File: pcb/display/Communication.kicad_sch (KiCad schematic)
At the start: 12 parts, among them U5 SP3485EN, U7 Ai-Thinker-Ra-02, U8 E220-400M22S

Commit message: Final Version of Prototype Rev. 00
Switched back to PCA9685 for PWM, removed high side switch
Updated some component values
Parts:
- R11, U7: now not fitted
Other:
- note removed: "OK!"
- title: (none) -> Communication
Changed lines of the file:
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@@
 	(paper "A4")
 	(title_block
-		(date "2024-11-11")
+		(title "Communication")
+		(date "2024-11-17")
 		(rev "00")
 		(company "Ravenspark")
@@
 			(width 0)
 			(type default)
-		)
-	)
-	(text "OK!"
-		(exclude_from_sim no)
-		(at 146.05 41.91 0)
-		(effects
-			(font
-				(size 2.54 2.54)
-				(thickness 0.254)
-				(bold yes)
-				(color 255 176 0 1)
-			)
 		)
 	)
@@
 		(in_bom yes)
 		(on_board yes)
-		(dnp no)
+		(dnp yes)
 		(fields_autoplaced yes)
 		(property "Reference" "U7"
@@
 		(in_bom yes)
 		(on_board yes)
-		(dnp no)
+		(dnp yes)
 		(property "Reference" "R11"
 			(at 95.25 146.05 90)

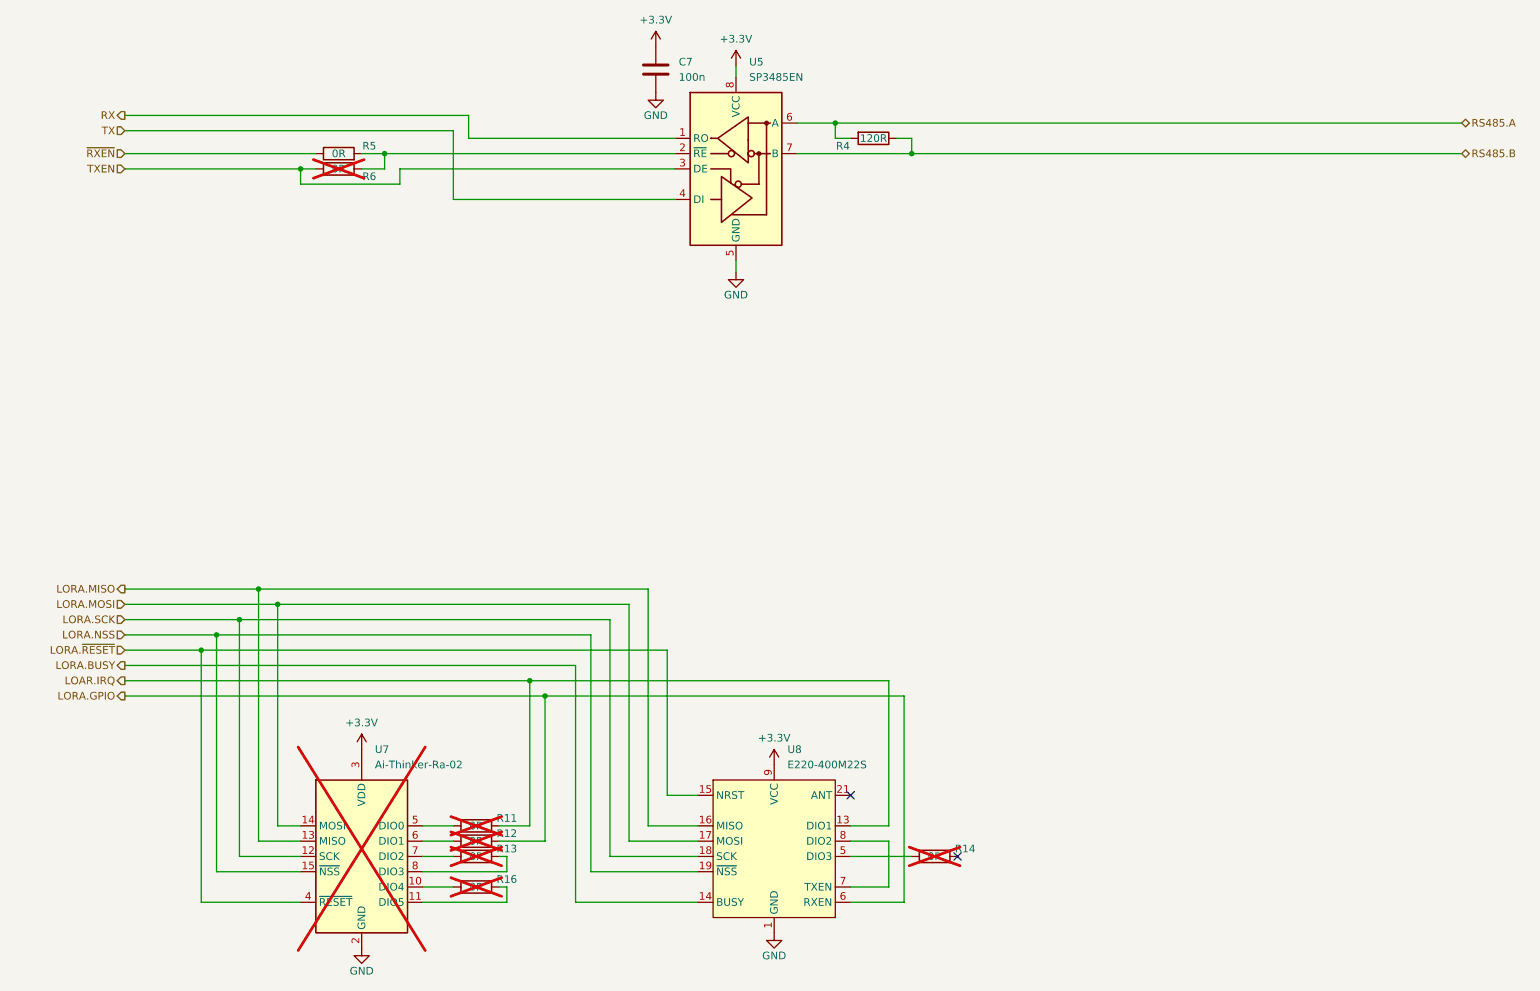
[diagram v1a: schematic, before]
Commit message: Display HW Revision 01
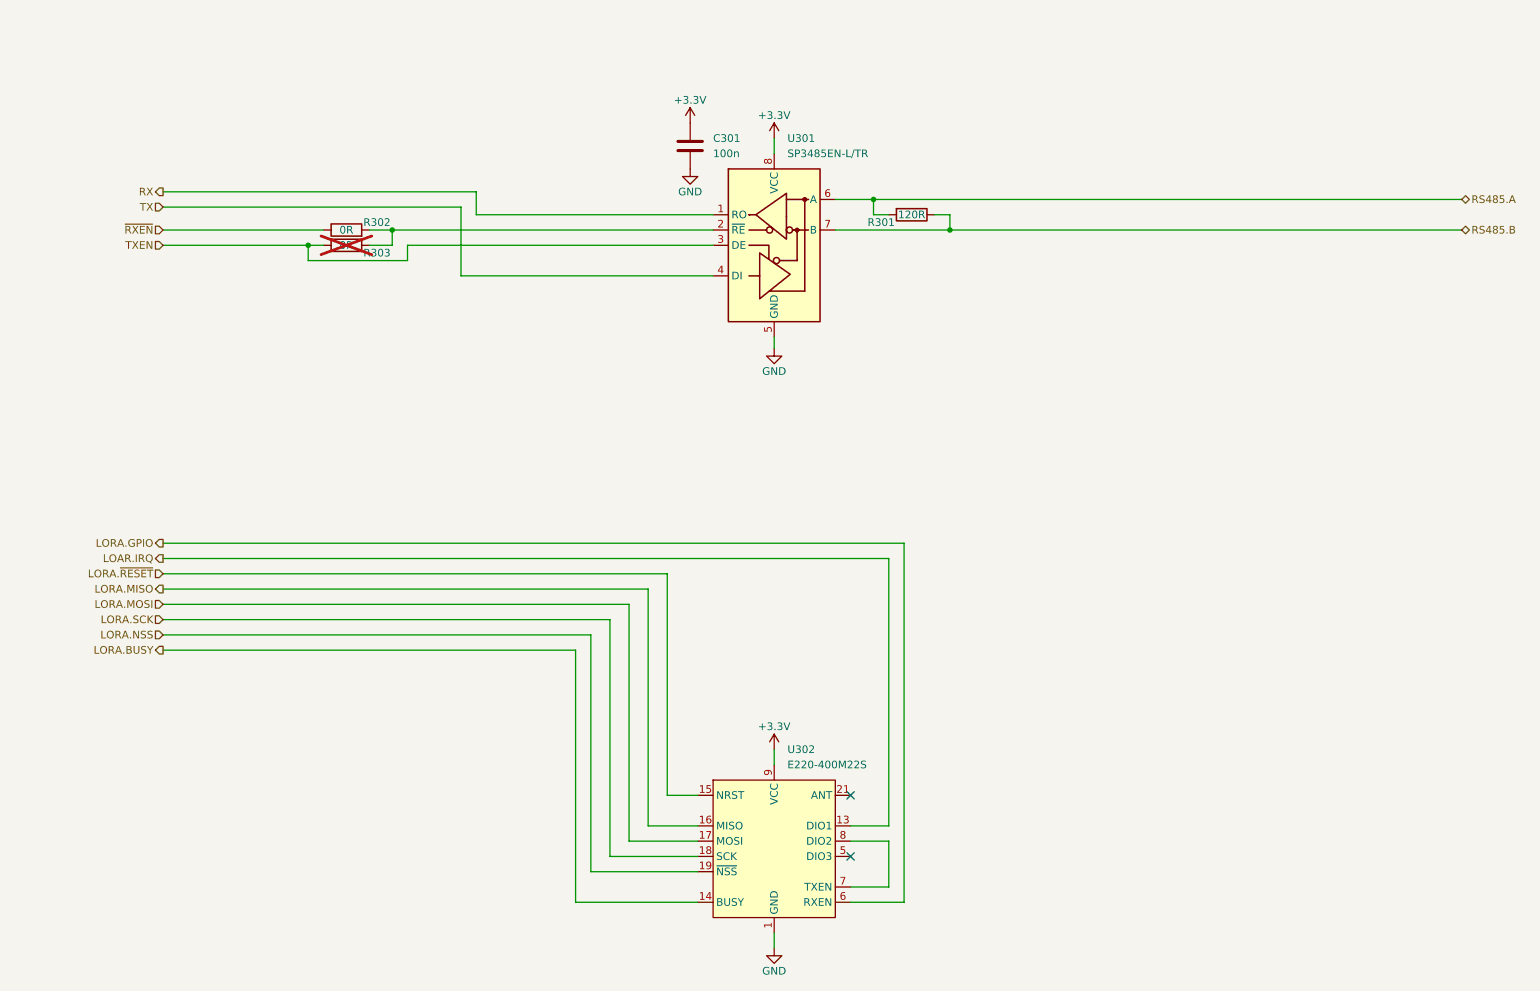
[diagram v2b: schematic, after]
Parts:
- removed R11, R12, R13, R14, R16: 0R, Resistor_SMD:R_0805_2012Metric, symbol Device:R
- removed U7: Ai-Thinker-Ra-02, RF_Module:Ai-Thinker-Ra-01-LoRa, symbol RF_Module:Ai-Thinker-Ra-02
- C301: renamed from C7; footprint Capacitor_SMD:C_0603_1608Metric -> Capacitor_SMD:C_0402_1005Metric; JLC PN (none) -> C307331
- U301: renamed from U5; value SP3485EN -> SP3485EN-L/TR; JLC PN (none) -> C8963
- U302: renamed from U8; JLC PN (none) -> C2971737
- renumbered R4 to R301, R5 to R302, R6 to R303
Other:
- moved on the sheet: C301, R301, R302, R303, U301

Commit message: OSC Display Hardware Revision 02
There might still be some errors which need to be corrected during ordering.
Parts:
- added C5: 1u, Capacitor_SMD:C_0402_1005Metric, symbol Device:C
- C301: JLC PN C307331 -> (none); LCSC Part # (none) -> C307331
- U301: JLC PN C8963 -> (none); LCSC Part # (none) -> C8963
- U302: JLC PN C2971737 -> (none); LCSC Part # (none) -> C2971737
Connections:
- net +3.3V: now also C5.1
- net GND: now also C5.2
